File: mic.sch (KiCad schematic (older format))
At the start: 8 parts, among them J7 JACK_TRS_5PINS

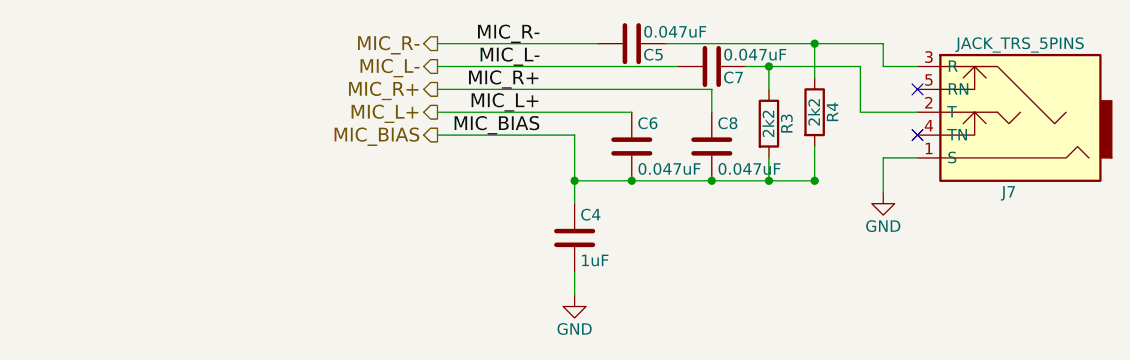
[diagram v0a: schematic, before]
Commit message: Major update to use Atmel ATTINY4313
Replace Pro Micro as microcontroller. Mostly contianed within the
control sheet.
Moved LEDs all onto control sheet.
Updated a few capacitors.
Added a reset switch. Still need to decide part.
Updated a few capacitor models for 4.0.7
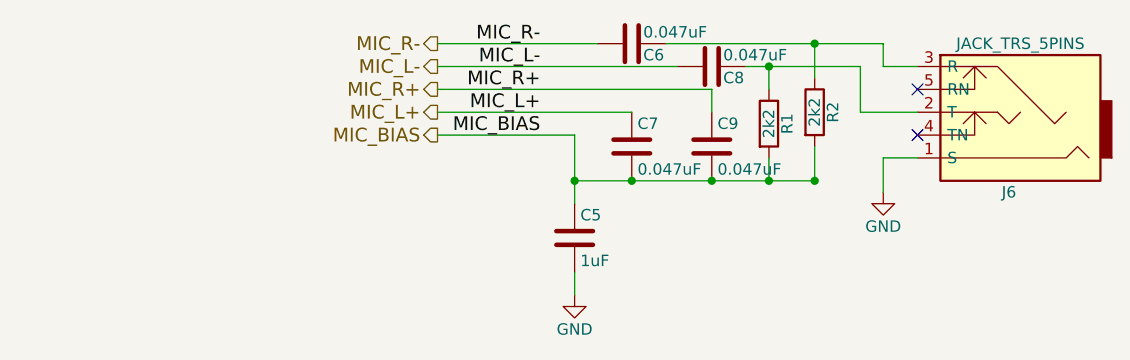
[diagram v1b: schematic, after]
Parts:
- renumbered C4 to C5, C5 to C6, C6 to C7, C7 to C8, C8 to C9, J7 to J6, R3 to R1, R4 to R2
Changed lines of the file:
@@
 $Descr USLetter 11000 8500
 encoding utf-8
-Sheet 7 10
+Sheet 6 10
 Title "Blubaru"
 Date "2017-02-28"
@@
 MIC_BIAS
 $Comp
-L C C7
+L C C8
 U 1 1 589D21D3
 P 5500 3750
-F 0 "C7" V 5550 3800 50  0000 L CNN
+F 0 "C8" V 5550 3800 50  0000 L CNN
 F 1 "0.047uF" V 5450 3800 50  0000 L CNN
 F 2 "blubaru:C_Disc_D4.0mm_W2.6mm_P2.50mm" H 5538 3600 50  0001 C CNN
@@
 $EndComp
 $Comp
-L C C6
+L C C7
 U 1 1 589D223D
 P 5150 4100
-F 0 "C6" H 5175 4200 50  0000 L CNN
+F 0 "C7" H 5175 4200 50  0000 L CNN
 F 1 "0.047uF" H 5175 4000 50  0000 L CNN
 F 2 "blubaru:C_Disc_D4.0mm_W2.6mm_P2.50mm" H 5188 3950 50  0001 C CNN
@@
 $EndComp
 $Comp
-L C C8
+L C C9
 U 1 1 589D230D
 P 5500 4100
-F 0 "C8" H 5525 4200 50  0000 L CNN
+F 0 "C9" H 5525 4200 50  0000 L CNN
 F 1 "0.047uF" H 5525 4000 50  0000 L CNN
 F 2 "blubaru:C_Disc_D4.0mm_W2.6mm_P2.50mm" H 5538 3950 50  0001 C CNN
@@
 $EndComp
 $Comp
-L C C4
+L C C5
 U 1 1 589D2382
 P 4900 4500
-F 0 "C4" H 4925 4600 50  0000 L CNN
+F 0 "C5" H 4925 4600 50  0000 L CNN
 F 1 "1uF" H 4925 4400 50  0000 L CNN
 F 2 "blubaru:C_Disc_D5.0mm_W3.2mm_P2.50mm" H 4938 4350 50  0001 C CNN
@@
 $EndComp
 $Comp
-L C C5
+L C C6
 U 1 1 589D23FA
 P 5150 3650
-F 0 "C5" V 5200 3700 50  0000 L CNN
+F 0 "C6" V 5200 3700 50  0000 L CNN
 F 1 "0.047uF" V 5100 3700 50  0000 L CNN
 F 2 "blubaru:C_Disc_D4.0mm_W2.6mm_P2.50mm" H 5188 3500 50  0001 C CNN
@@
 $EndComp
 $Comp
-L R R3
+L R R1
 U 1 1 589D2492
 P 5750 4000
-F 0 "R3" V 5830 4000 50  0000 C CNN
+F 0 "R1" V 5830 4000 50  0000 C CNN
 F 1 "2k2" V 5750 4000 50  0000 C CNN
 F 2 "Resistors_THT:R_Axial_DIN0204_L3.6mm_D1.6mm_P5.08mm_Horizontal" V 5680 4000 50  0001 C CNN
@@
 $EndComp
 $Comp
-L R R4
+L R R2
 U 1 1 589D2525
 P 5950 3950
-F 0 "R4" V 6030 3950 50  0000 C CNN
+F 0 "R2" V 6030 3950 50  0000 C CNN
 F 1 "2k2" V 5950 3950 50  0000 C CNN
 F 2 "Resistors_THT:R_Axial_DIN0204_L3.6mm_D1.6mm_P5.08mm_Horizontal" V 5880 3950 50  0001 C CNN
@@
 $EndComp
 $Comp
-L GND #PWR026
+L GND #PWR021
 U 1 1 589D259B
 P 4900 4750
-F 0 "#PWR026" H 4900 4500 50  0001 C CNN
+F 0 "#PWR021" H 4900 4500 50  0001 C CNN
 F 1 "GND" H 4900 4600 50  0000 C CNN
 F 2 "" H 4900 4750 50  0000 C CNN
@@
 $EndComp
 $Comp
-L GND #PWR027
+L GND #PWR022
 U 1 1 589E6671
 P 6250 4300
-F 0 "#PWR027" H 6250 4050 50  0001 C CNN
+F 0 "#PWR022" H 6250 4050 50  0001 C CNN
 F 1 "GND" H 6250 4150 50  0000 C CNN
 F 2 "" H 6250 4300 50  0000 C CNN
@@
 MIC_BIAS
 $Comp
-L JACK_TRS_5PINS J7
+L JACK_TRS_5PINS J6
 U 1 1 58BF91C1
 P 6800 3950
-F 0 "J7" H 6800 4300 50  0000 C CNN
+F 0 "J6" H 6800 4300 50  0000 C CNN
 F 1 "JACK_TRS_5PINS" H 6750 3650 50  0000 C CNN
 F 2 "blubaru:sj1-353xng" H 6900 3800 50  0001 C CNN
-F 3 "http://www.cui.com/product/resource/sj1-352xng-series.pdf" H 6900 3800 50  0001 C CNN
+F 3 "http://www.cui.com/product/resource/sj1-353xng.pdf" H 6900 3800 50  0001 C CNN
 	1    6800 3950
 	-1   0    0    1

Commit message: Add LEDs to BT module
These already exist on the breakout board, but they will be more visible
if I add resistors to the front panel. They can be removed if space is
limited and the case is translucent, but add them for now. In V2, there
won't be a breakout board, so adding them now makes the V1 to V2 fewer
changes.
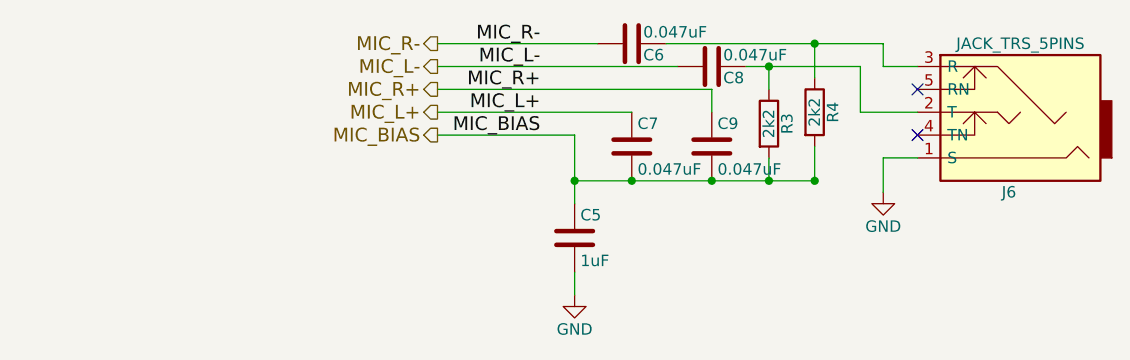
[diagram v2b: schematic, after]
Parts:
- renumbered R1 to R3, R2 to R4
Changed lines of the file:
@@
 $EndComp
 $Comp
-L R R1
+L R R3
 U 1 1 589D2492
 P 5750 4000
-F 0 "R1" V 5830 4000 50  0000 C CNN
+F 0 "R3" V 5830 4000 50  0000 C CNN
 F 1 "2k2" V 5750 4000 50  0000 C CNN
 F 2 "Resistors_THT:R_Axial_DIN0204_L3.6mm_D1.6mm_P5.08mm_Horizontal" V 5680 4000 50  0001 C CNN
@@
 $EndComp
 $Comp
-L R R2
+L R R4
 U 1 1 589D2525
 P 5950 3950
-F 0 "R2" V 6030 3950 50  0000 C CNN
+F 0 "R4" V 6030 3950 50  0000 C CNN
 F 1 "2k2" V 5950 3950 50  0000 C CNN
 F 2 "Resistors_THT:R_Axial_DIN0204_L3.6mm_D1.6mm_P5.08mm_Horizontal" V 5880 3950 50  0001 C CNN
@@
 $EndComp
 $Comp
-L GND #PWR021
+L GND #PWR022
 U 1 1 589D259B
 P 4900 4750
-F 0 "#PWR021" H 4900 4500 50  0001 C CNN
+F 0 "#PWR022" H 4900 4500 50  0001 C CNN
 F 1 "GND" H 4900 4600 50  0000 C CNN
 F 2 "" H 4900 4750 50  0000 C CNN
@@
 $EndComp
 $Comp
-L GND #PWR022
+L GND #PWR023
 U 1 1 589E6671
 P 6250 4300
-F 0 "#PWR022" H 6250 4050 50  0001 C CNN
+F 0 "#PWR023" H 6250 4050 50  0001 C CNN
 F 1 "GND" H 6250 4150 50  0000 C CNN
 F 2 "" H 6250 4300 50  0000 C CNN

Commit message: Clean up some schematics for readability.
Run 12V from after power protection diode.
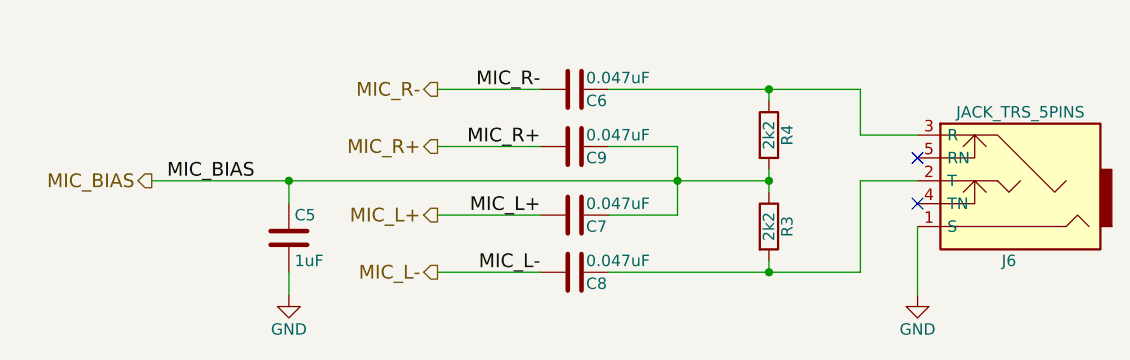
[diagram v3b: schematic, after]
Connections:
- net MIC_BIAS: now also C7.1, C9.1, R3.1; no longer C7.2, C9.2, R3.2
- net MIC_L+: now also C7.2; no longer C7.1
- net MIC_R+: now also C9.2; no longer C9.1
- net at C8.1, J6.2 (T): now also R3.2; no longer R3.1
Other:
- moved on the sheet: C5, C6, C7, C8, C9, J6, R3, R4
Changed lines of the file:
@@
 Comment4 ""
 $EndDescr
-Text Label 4750 3650 2    60   ~ 0
+Text Label 4750 3850 2    60   ~ 0
 MIC_R-
-Text Label 4750 3850 2    60   ~ 0
+Text Label 4750 4100 2    60   ~ 0
 MIC_R+
-Text Label 4750 3750 2    60   ~ 0
+Text Label 4750 4650 2    60   ~ 0
 MIC_L-
-Text Label 4750 3950 2    60   ~ 0
+Text Label 4750 4400 2    60   ~ 0
 MIC_L+
-Text Label 4750 4050 2    60   ~ 0
+Text Label 3500 4250 2    60   ~ 0
 MIC_BIAS
 $Comp
 L C C8
 U 1 1 589D21D3
-P 5500 3750
-F 0 "C8" V 5550 3800 50  0000 L CNN
-F 1 "0.047uF" V 5450 3800 50  0000 L CNN
-F 2 "blubaru:C_Disc_D4.0mm_W2.6mm_P2.50mm" H 5538 3600 50  0001 C CNN
-F 3 "http://www.vishay.com/docs/45171/kseries.pdf" H 5500 3750 50  0001 C CNN
-	1    5500 3750
+P 4900 4650
+F 0 "C8" V 4950 4700 50  0000 L CNN
+F 1 "0.047uF" V 4850 4700 50  0000 L CNN
+F 2 "blubaru:C_Disc_D4.0mm_W2.6mm_P2.50mm" H 4938 4500 50  0001 C CNN
+F 3 "http://www.vishay.com/docs/45171/kseries.pdf" H 4900 4650 50  0001 C CNN
+	1    4900 4650
 	0    1    1    0
 $EndComp
@@
 L C C7
 U 1 1 589D223D
-P 5150 4100
-F 0 "C7" H 5175 4200 50  0000 L CNN
-F 1 "0.047uF" H 5175 4000 50  0000 L CNN
-F 2 "blubaru:C_Disc_D4.0mm_W2.6mm_P2.50mm" H 5188 3950 50  0001 C CNN
-F 3 "http://www.vishay.com/docs/45171/kseries.pdf" H 5150 4100 50  0001 C CNN
-	1    5150 4100
-	1    0    0    -1
+P 4900 4400
+F 0 "C7" V 4950 4450 50  0000 L CNN
+F 1 "0.047uF" V 4850 4450 50  0000 L CNN
+F 2 "blubaru:C_Disc_D4.0mm_W2.6mm_P2.50mm" H 4938 4250 50  0001 C CNN
+F 3 "http://www.vishay.com/docs/45171/kseries.pdf" H 4900 4400 50  0001 C CNN
+	1    4900 4400
+	0    1    1    0
 $EndComp
 $Comp
 L C C9
 U 1 1 589D230D
-P 5500 4100
-F 0 "C9" H 5525 4200 50  0000 L CNN
-F 1 "0.047uF" H 5525 4000 50  0000 L CNN
-F 2 "blubaru:C_Disc_D4.0mm_W2.6mm_P2.50mm" H 5538 3950 50  0001 C CNN
-F 3 "http://www.vishay.com/docs/45171/kseries.pdf" H 5500 4100 50  0001 C CNN
-	1    5500 4100
-	1    0    0    -1
+P 4900 4100
+F 0 "C9" V 4950 4150 50  0000 L CNN
+F 1 "0.047uF" V 4850 4150 50  0000 L CNN
+F 2 "blubaru:C_Disc_D4.0mm_W2.6mm_P2.50mm" H 4938 3950 50  0001 C CNN
+F 3 "http://www.vishay.com/docs/45171/kseries.pdf" H 4900 4100 50  0001 C CNN
+	1    4900 4100
+	0    1    1    0
 $EndComp
 $Comp
 L C C5
 U 1 1 589D2382
-P 4900 4500
-F 0 "C5" H 4925 4600 50  0000 L CNN
-F 1 "1uF" H 4925 4400 50  0000 L CNN
-F 2 "blubaru:C_Disc_D5.0mm_W3.2mm_P2.50mm" H 4938 4350 50  0001 C CNN
-F 3 "http://www.vishay.com/docs/45171/kseries.pdf" H 4900 4500 50  0001 C CNN
-	1    4900 4500
+P 3650 4500
+F 0 "C5" H 3675 4600 50  0000 L CNN
+F 1 "1uF" H 3675 4400 50  0000 L CNN
+F 2 "blubaru:C_Disc_D5.0mm_W3.2mm_P2.50mm" H 3688 4350 50  0001 C CNN
+F 3 "http://www.vishay.com/docs/45171/kseries.pdf" H 3650 4500 50  0001 C CNN
+	1    3650 4500
 	1    0    0    -1
 $EndComp
@@
 L C C6
 U 1 1 589D23FA
-P 5150 3650
-F 0 "C6" V 5200 3700 50  0000 L CNN
-F 1 "0.047uF" V 5100 3700 50  0000 L CNN
-F 2 "blubaru:C_Disc_D4.0mm_W2.6mm_P2.50mm" H 5188 3500 50  0001 C CNN
-F 3 "http://www.vishay.com/docs/45171/kseries.pdf" H 5150 3650 50  0001 C CNN
-	1    5150 3650
+P 4900 3850
+F 0 "C6" V 4950 3900 50  0000 L CNN
+F 1 "0.047uF" V 4850 3900 50  0000 L CNN
+F 2 "blubaru:C_Disc_D4.0mm_W2.6mm_P2.50mm" H 4938 3700 50  0001 C CNN
+F 3 "http://www.vishay.com/docs/45171/kseries.pdf" H 4900 3850 50  0001 C CNN
+	1    4900 3850
 	0    1    1    0
 $EndComp
@@
 L R R3
 U 1 1 589D2492
-P 5750 4000
-F 0 "R3" V 5830 4000 50  0000 C CNN
-F 1 "2k2" V 5750 4000 50  0000 C CNN
-F 2 "Resistors_THT:R_Axial_DIN0204_L3.6mm_D1.6mm_P5.08mm_Horizontal" V 5680 4000 50  0001 C CNN
-F 3 "https://www.seielect.com/Catalog/SEI-RNF_RNMF.pdf" H 5750 4000 50  0001 C CNN
-	1    5750 4000
+P 5750 4450
+F 0 "R3" V 5830 4450 50  0000 C CNN
+F 1 "2k2" V 5750 4450 50  0000 C CNN
+F 2 "Resistors_THT:R_Axial_DIN0204_L3.6mm_D1.6mm_P5.08mm_Horizontal" V 5680 4450 50  0001 C CNN
+F 3 "https://www.seielect.com/Catalog/SEI-RNF_RNMF.pdf" H 5750 4450 50  0001 C CNN
+	1    5750 4450
 	1    0    0    -1
 $EndComp
@@
 L R R4
 U 1 1 589D2525
-P 5950 3950
-F 0 "R4" V 6030 3950 50  0000 C CNN
-F 1 "2k2" V 5950 3950 50  0000 C CNN
-F 2 "Resistors_THT:R_Axial_DIN0204_L3.6mm_D1.6mm_P5.08mm_Horizontal" V 5880 3950 50  0001 C CNN
-F 3 "https://www.seielect.com/Catalog/SEI-RNF_RNMF.pdf" H 5950 3950 50  0001 C CNN
-	1    5950 3950
+P 5750 4050
+F 0 "R4" V 5830 4050 50  0000 C CNN
+F 1 "2k2" V 5750 4050 50  0000 C CNN
+F 2 "Resistors_THT:R_Axial_DIN0204_L3.6mm_D1.6mm_P5.08mm_Horizontal" V 5680 4050 50  0001 C CNN
+F 3 "https://www.seielect.com/Catalog/SEI-RNF_RNMF.pdf" H 5750 4050 50  0001 C CNN
+	1    5750 4050
 	1    0    0    -1
 $EndComp
@@
 L GND #PWR022
 U 1 1 589D259B
-P 4900 4750
-F 0 "#PWR022" H 4900 4500 50  0001 C CNN
-F 1 "GND" H 4900 4600 50  0000 C CNN
-F 2 "" H 4900 4750 50  0000 C CNN
-F 3 "" H 4900 4750 50  0000 C CNN
-	1    4900 4750
+P 3650 4750
+F 0 "#PWR022" H 3650 4500 50  0001 C CNN
+F 1 "GND" H 3650 4600 50  0000 C CNN
+F 2 "" H 3650 4750 50  0000 C CNN
+F 3 "" H 3650 4750 50  0000 C CNN
+	1    3650 4750
 	1    0    0    -1
 $EndComp
@@
 L GND #PWR023
 U 1 1 589E6671
-P 6250 4300
-F 0 "#PWR023" H 6250 4050 50  0001 C CNN
-F 1 "GND" H 6250 4150 50  0000 C CNN
-F 2 "" H 6250 4300 50  0000 C CNN
-F 3 "" H 6250 4300 50  0000 C CNN
-	1    6250 4300
+P 6400 4750
+F 0 "#PWR023" H 6400 4500 50  0001 C CNN
+F 1 "GND" H 6400 4600 50  0000 C CNN
+F 2 "" H 6400 4750 50  0000 C CNN
+F 3 "" H 6400 4750 50  0000 C CNN
+	1    6400 4750
 	1    0    0    -1
 $EndComp
 Wire Wire Line
-	4300 3650 5000 3650
+	4300 3850 4750 3850
 Wire Wire Line
-	4300 3750 5350 3750
+	4300 4650 4750 4650
 Wire Wire Line
-	4300 3850 5500 3850
+	3050 4250 5750 4250
 Wire Wire Line
-	4300 3950 5150 3950
+	3650 4650 3650 4750
 Wire Wire Line
-	4300 4050 4900 4050
+	3650 4250 3650 4350
+Connection ~ 3650 4250
+Connection ~ 5350 4250
 Wire Wire Line
-	4900 4650 4900 4750
-Wire Wire Line
-	4900 4050 4900 4350
-Wire Wire Line
-	5500 3850 5500 3950
-Connection ~ 4900 4250
-Connection ~ 5150 4250
-Connection ~ 5500 4250
-Wire Wire Line
-	5650 3750 6150 3750
+	5050 4650 6150 4650
 Connection ~ 5750 4250
 Wire Wire Line
-	5300 3650 6250 3650
+	5050 3850 6150 3850
 Wire Wire Line
-	5750 3750 5750 3850
+	5750 3850 5750 3900
 Wire Wire Line
-	5750 4250 5750 4150
+	5750 4200 5750 4300
+Connection ~ 5750 3850
+Connection ~ 5750 4650
 Wire Wire Line
-	5950 3650 5950 3800
+	6150 4250 6400 4250
 Wire Wire Line
-	5950 4250 5950 4100
-Connection ~ 5950 4250
-Connection ~ 5950 3650
-Connection ~ 5750 3750
+	6150 3850 6150 4050
 Wire Wire Line
-	4900 4250 5950 4250
-Wire Wire Line
-	6150 3750 6150 3950
-Wire Wire Line
-	6150 3950 6400 3950
-Wire Wire Line
-	6250 3650 6250 3750
-Wire Wire Line
-	6250 3750 6400 3750
-Wire Wire Line
-	6400 4150 6250 4150
-Wire Wire Line
-	6250 4150 6250 4300
-NoConn ~ 6400 3850
-NoConn ~ 6400 4050
-Text HLabel 4300 3650 0    60   Output ~ 0
+	6150 4050 6400 4050
+NoConn ~ 6400 4150
+NoConn ~ 6400 4350
+Text HLabel 4300 3850 0    60   Output ~ 0
 MIC_R-
-Text HLabel 4300 3750 0    60   Output ~ 0
+Text HLabel 4300 4650 0    60   Output ~ 0
 MIC_L-
-Text HLabel 4300 3850 0    60   Output ~ 0
+Text HLabel 4300 4100 0    60   Output ~ 0
 MIC_R+
-Text HLabel 4300 3950 0    60   Output ~ 0
+Text HLabel 4300 4400 0    60   Output ~ 0
 MIC_L+
-Text HLabel 4300 4050 0    60   Output ~ 0
+Text HLabel 3050 4250 0    60   Output ~ 0
 MIC_BIAS
 $Comp
 L JACK_TRS_5PINS J6
 U 1 1 58BF91C1
-P 6800 3950
-F 0 "J6" H 6800 4300 50  0000 C CNN
-F 1 "JACK_TRS_5PINS" H 6750 3650 50  0000 C CNN
-F 2 "blubaru:sj1-353xng" H 6900 3800 50  0001 C CNN
-F 3 "http://www.cui.com/product/resource/sj1-353xng.pdf" H 6900 3800 50  0001 C CNN
-	1    6800 3950
+P 6800 4250
+F 0 "J6" H 6800 4600 50  0000 C CNN
+F 1 "JACK_TRS_5PINS" H 6750 3950 50  0000 C CNN
+F 2 "blubaru:sj1-353xng" H 6900 4100 50  0001 C CNN
+F 3 "http://www.cui.com/product/resource/sj1-353xng.pdf" H 6900 4100 50  0001 C CNN
+	1    6800 4250
 	-1   0    0    1
 $EndComp
+Wire Wire Line
+	6150 4650 6150 4250
+Wire Wire Line
+	5750 4600 5750 4650
+Wire Wire Line
+	4300 4100 4750 4100
+Wire Wire Line
+	4300 4400 4750 4400
+Wire Wire Line
+	5050 4100 5350 4100
+Wire Wire Line
+	5350 4100 5350 4400
+Wire Wire Line
+	5350 4400 5050 4400
+Wire Wire Line
+	6400 4450 6400 4750
 $EndSCHEMATC

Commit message: Rename the bluetooth reset line
This is needed so it doesn't conflict with the MCU reset line of the
same name. Apparently that puts them on the same net.

Also, reorder the LEDs so they have nicer numbers on the board.
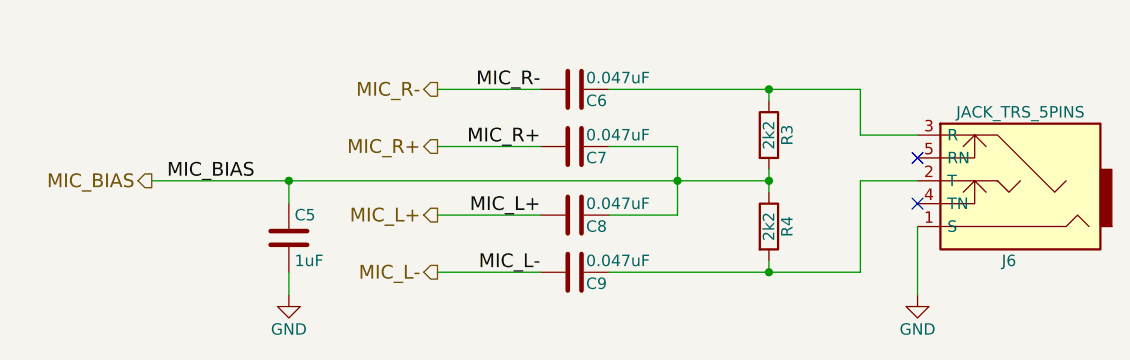
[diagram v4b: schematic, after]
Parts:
- renumbered C9 to C7, C7 to C8, C8 to C9, R4 to R3, R3 to R4
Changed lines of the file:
@@
 MIC_BIAS
 $Comp
-L C C8
+L C C9
 U 1 1 589D21D3
 P 4900 4650
-F 0 "C8" V 4950 4700 50  0000 L CNN
+F 0 "C9" V 4950 4700 50  0000 L CNN
 F 1 "0.047uF" V 4850 4700 50  0000 L CNN
 F 2 "blubaru:C_Disc_D4.0mm_W2.6mm_P2.50mm" H 4938 4500 50  0001 C CNN
@@
 $EndComp
 $Comp
-L C C7
+L C C8
 U 1 1 589D223D
 P 4900 4400
-F 0 "C7" V 4950 4450 50  0000 L CNN
+F 0 "C8" V 4950 4450 50  0000 L CNN
 F 1 "0.047uF" V 4850 4450 50  0000 L CNN
 F 2 "blubaru:C_Disc_D4.0mm_W2.6mm_P2.50mm" H 4938 4250 50  0001 C CNN
@@
 $EndComp
 $Comp
-L C C9
+L C C7
 U 1 1 589D230D
 P 4900 4100
-F 0 "C9" V 4950 4150 50  0000 L CNN
+F 0 "C7" V 4950 4150 50  0000 L CNN
 F 1 "0.047uF" V 4850 4150 50  0000 L CNN
 F 2 "blubaru:C_Disc_D4.0mm_W2.6mm_P2.50mm" H 4938 3950 50  0001 C CNN
@@
 $EndComp
 $Comp
-L R R3
+L R R4
 U 1 1 589D2492
 P 5750 4450
-F 0 "R3" V 5830 4450 50  0000 C CNN
+F 0 "R4" V 5830 4450 50  0000 C CNN
 F 1 "2k2" V 5750 4450 50  0000 C CNN
 F 2 "Resistors_THT:R_Axial_DIN0204_L3.6mm_D1.6mm_P5.08mm_Horizontal" V 5680 4450 50  0001 C CNN
@@
 $EndComp
 $Comp
-L R R4
+L R R3
 U 1 1 589D2525
 P 5750 4050
-F 0 "R4" V 5830 4050 50  0000 C CNN
+F 0 "R3" V 5830 4050 50  0000 C CNN
 F 1 "2k2" V 5750 4050 50  0000 C CNN
 F 2 "Resistors_THT:R_Axial_DIN0204_L3.6mm_D1.6mm_P5.08mm_Horizontal" V 5680 4050 50  0001 C CNN
